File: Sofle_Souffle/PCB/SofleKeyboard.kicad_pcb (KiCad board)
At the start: 2 copper layers, 143.3 x 111.7 mm, 91 parts, among them J2 4PIN, J3 OLED, J4 Conn_01x05_Female, P1 i2c_pin, P2 i2c_pin, SW1 SW_PUSH-MX_W_LED, SW10 SW_PUSH-MX_W_LED, SW11 SW_PUSH-MX_W_LED, SW12 SW_PUSH-MX_W_LED, SW13 SW_PUSH-MX_W_LED, SW14 SW_PUSH-MX_W_LED, SW15 SW_PUSH-MX_W_LED, SW16 SW_PUSH-MX_W_LED, SW17 SW_PUSH-MX_W_LED, SW18 SW_PUSH-MX_W_LED, SW19 SW_PUSH-MX_W_LED, SW2 SW_PUSH-MX_W_LED, SW20 SW_PUSH-MX_W_LED, SW21 SW_PUSH-MX_W_LED, SW22 SW_PUSH-MX_W_LED, SW23 SW_PUSH-MX_W_LED, SW24 SW_PUSH-MX_W_LED, SW25 Rotary_Encoder_Switch, SW26 SW_PUSH-MX_W_LED, SW27 SW_PUSH-MX_W_LED, SW28 SW_PUSH-MX_W_LED, SW29 SW_PUSH-MX_W_LED, SW3 SW_PUSH-MX_W_LED, SW30 SW_PUSH-MX_W_LED, SW4 SW_PUSH-MX_W_LED, SW5 SW_PUSH-MX_W_LED, SW6 SW_PUSH-MX_W_LED, SW7 SW_PUSH-MX_W_LED, SW8 SW_PUSH-MX_W_LED, SW9 SW_PUSH-MX_W_LED, U1 ProMicro

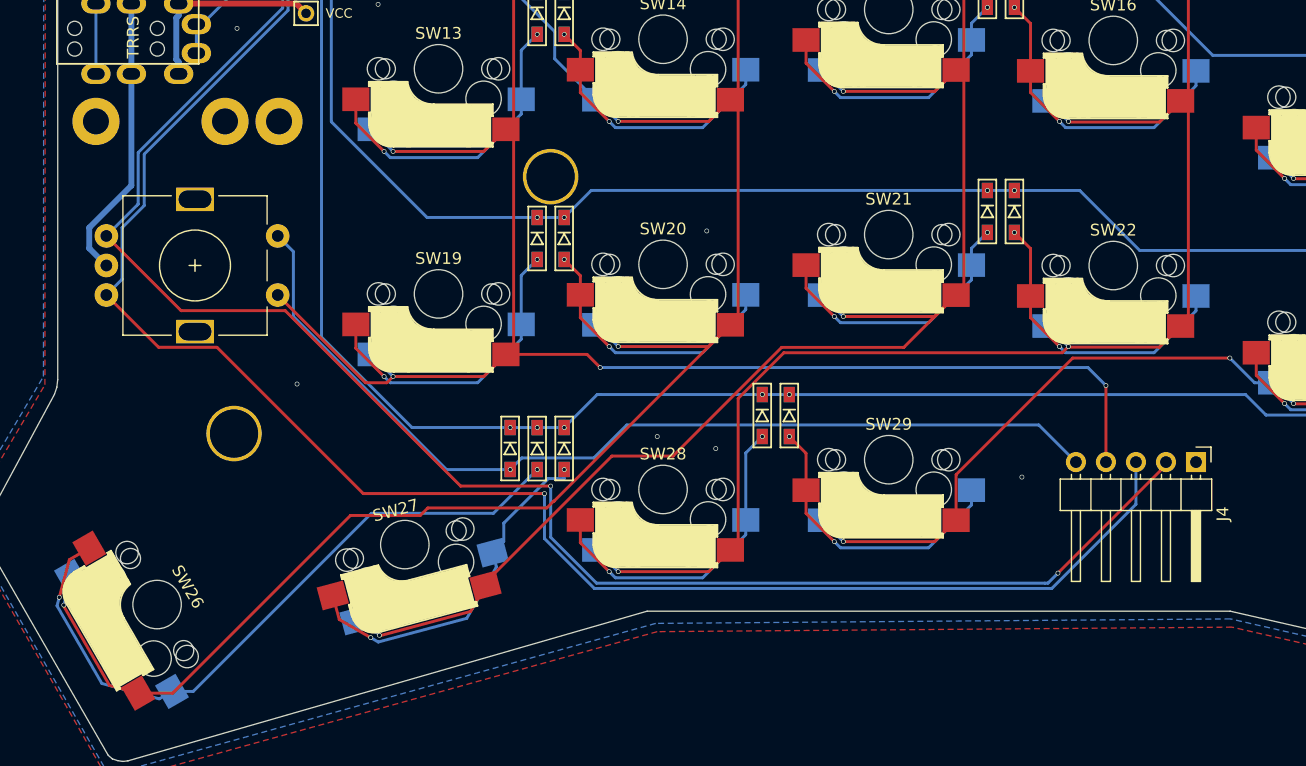
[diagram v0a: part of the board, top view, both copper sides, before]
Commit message: Removed 5pin connector on the right side of the case/pcb.
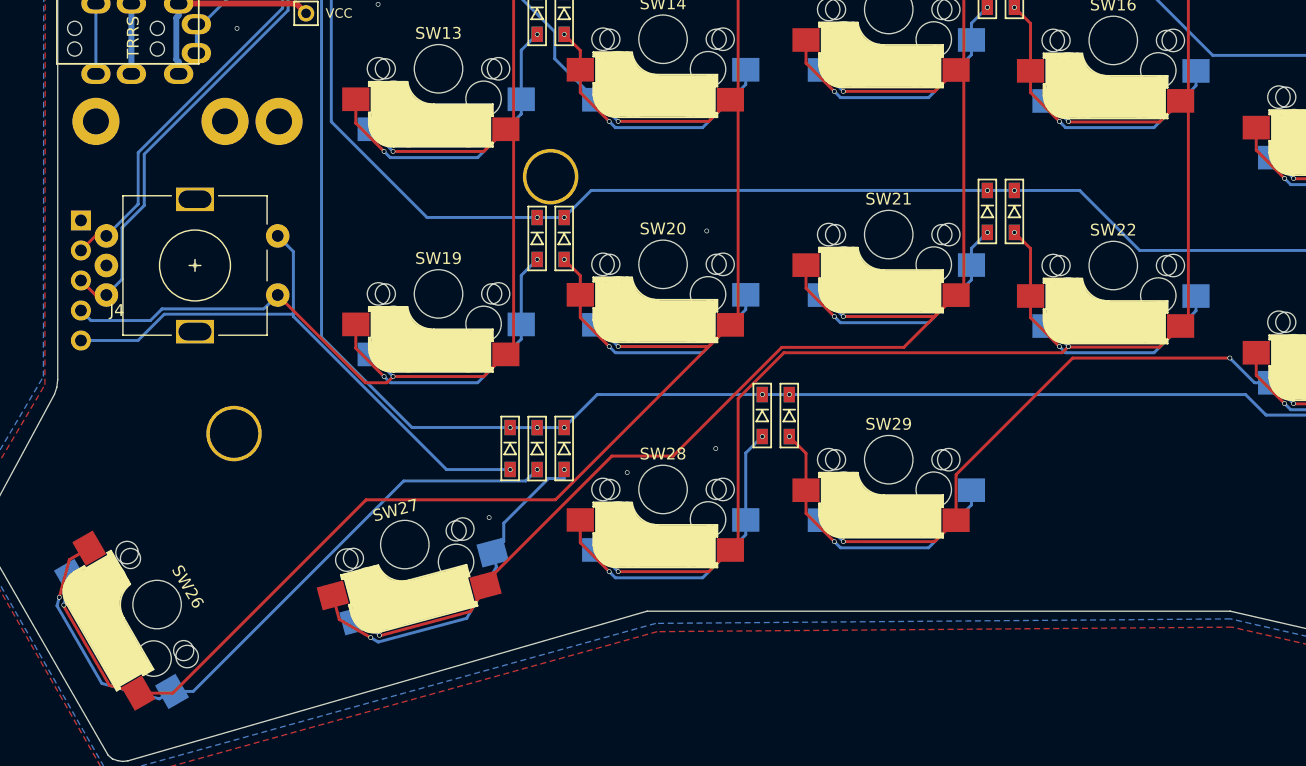
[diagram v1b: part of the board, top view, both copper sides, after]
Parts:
- J4: moved to B.Cu
- moved J4 96.6 mm to (83.6, 103.1), turned to 180 degrees
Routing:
- net ENCA: track 180.9 -> 74.8 mm, vias 3 -> 1
- net ENCB: track 180.9 -> 77.4 mm, vias 2 -> 1
- net SW25A: track 211.5 -> 171.0 mm, vias 6 -> 4
- net SW25B: track 81.8 -> 50.0 mm
- net GND: track 114.2 -> 95.9 mm

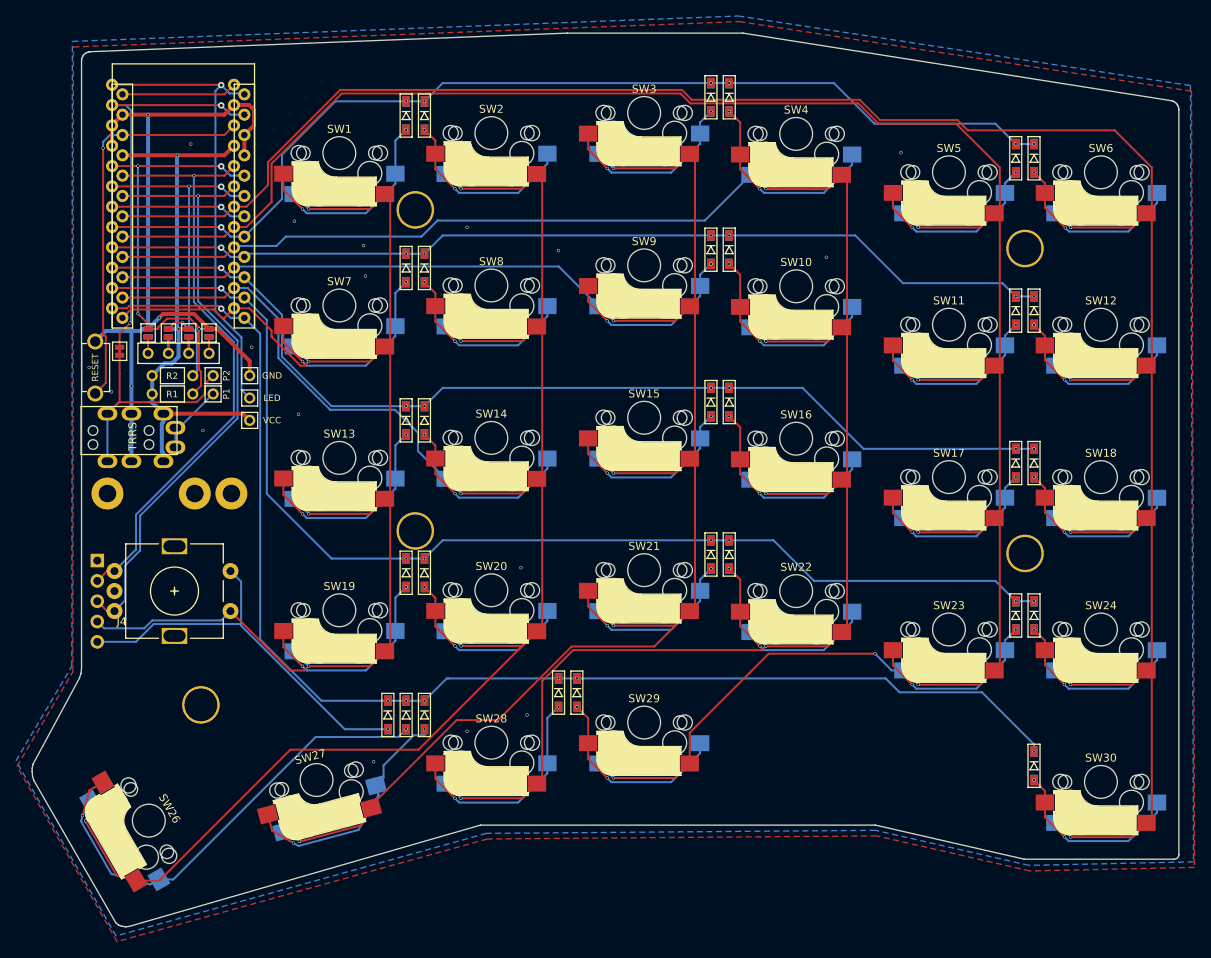
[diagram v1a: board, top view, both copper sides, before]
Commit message: Moved the connector pins for the roller encoder.
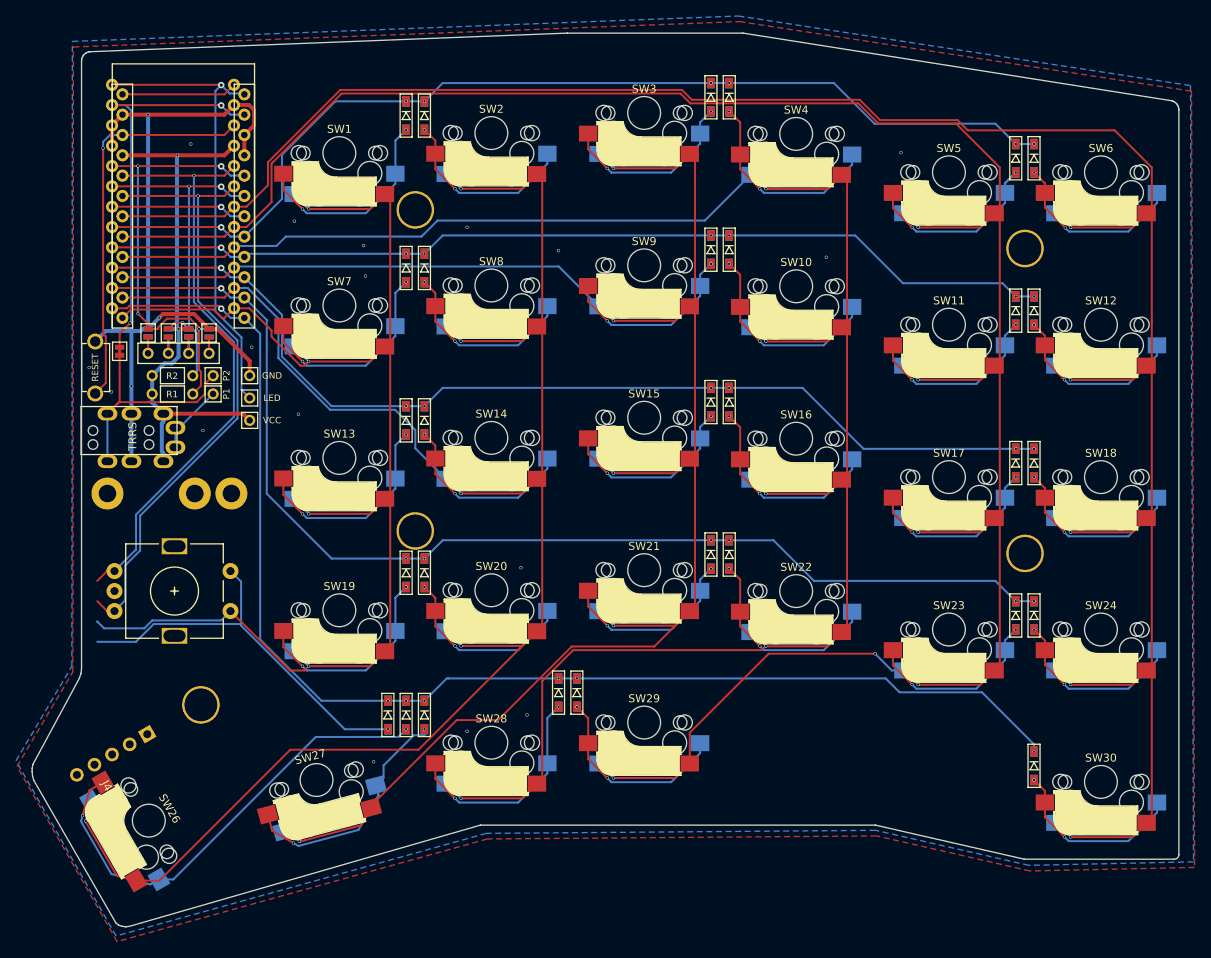
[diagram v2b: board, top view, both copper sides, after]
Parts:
- moved J4 22.6 mm to (89.8, 124.8), turned to 120 degrees
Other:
- net class Default removed
- net class GND removed
- net class VCC removed

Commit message: Moved roller encoder connectors to the same vertical location.
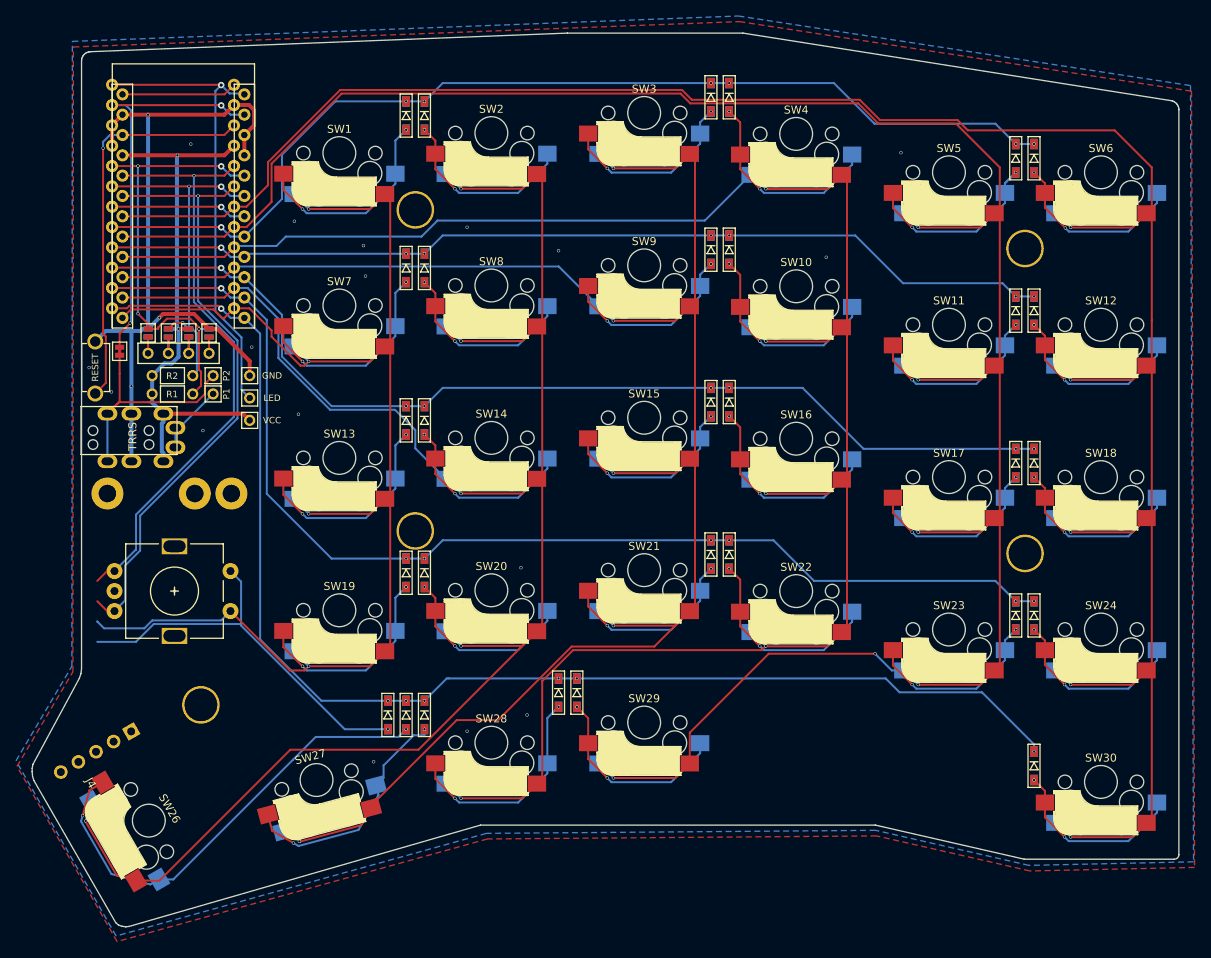
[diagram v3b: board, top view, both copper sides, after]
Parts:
- J4: footprint Connector_PinHeader_2.54mm:PinHeader_1x05_P2.54mm_Horizontal -> SofleRGB:PinHeader_1x05_P2.54mm_Horizontal
- SW1, SW10, SW11, SW12, SW13, SW14, SW15, SW16, SW17, SW18, SW19, SW2, SW20, SW21, SW22, SW23, SW24, SW26, SW27, SW28, SW29, SW3, SW30, SW4, SW5, SW6, SW7, SW8, SW9: footprint SofleRGB:SK6812MINI_and_cherry_NoLEDPads -> SofleRGB:SK6812MINI_and_cherry_NoLEDPads_Narrow_switch_holes
- moved J4 2.04 mm to (87.8, 124.5)

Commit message: Small updates on the PCB and case.
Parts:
- added P3: i2c_pin, SofleRGB:1pin_conn, F.Cu at (97.8, 91.2)
- added P4: i2c_pin, SofleRGB:1pin_conn, F.Cu at (100.6, 91.2)
- added P5: i2c_pin, SofleRGB:1pin_conn, F.Cu at (96.5, 88.4)
- added P6: i2c_pin, SofleRGB:1pin_conn, F.Cu at (99.3, 88.4)
- added P7: i2c_pin, SofleRGB:1pin_conn, F.Cu at (102.1, 88.4)
- added P8: sw_pin, SofleRGB:Single_Hole, F.Cu at (100.8, 99.4)
- added P9: sw_pin, SofleRGB:Single_Hole, F.Cu at (98.2, 99.4)
- added SW25A1: SW_PUSH-MX_W_LED, SofleRGB:SK6812MINI_and_cherry_NoLEDPads, F.Cu at (93.2, 106.9)
- J4: footprint SofleRGB:PinHeader_1x05_P2.54mm_Horizontal -> Connector_PinHeader_2.54mm:PinHeader_1x05_P2.54mm_Horizontal
- SW1, SW10, SW11, SW12, SW13, SW14, SW15, SW16, SW17, SW18, SW19, SW2, SW20, SW21, SW22, SW23, SW24, SW26, SW27, SW28, SW29, SW3, SW30, SW4, SW5, SW6, SW7, SW8, SW9: footprint SofleRGB:SK6812MINI_and_cherry_NoLEDPads_Narrow_switch_holes -> SofleRGB:SK6812MINI_and_cherry_NoLEDPads
- turned SW25 to -90 degrees
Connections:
- U1 pad 24: Net-(U1-Pad24) -> unconnected-(U1-Pad24)
- U1 pad 7: Net-(U1-Pad7) -> unconnected-(U1-Pad7)
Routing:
- net SW25B: track 50.0 -> 88.3 mm, vias 1 -> 2
- net SW25A: track 171.0 -> 207.1 mm
- net ENCA: track 74.8 -> 98.3 mm
- net unconnected-(U1-Pad7): track 0.00 -> 17.0 mm, vias 0 -> 1
- net Net-(U1-Pad7): track 17.0 -> 0.00 mm, vias 1 -> 0
- net ENCB: track 77.4 -> 93.1 mm
- net unconnected-(U1-Pad24): track 0.00 -> 14.4 mm
- net Net-(U1-Pad24): track 14.4 -> 0.00 mm
- net col1: track 288.4 -> 294.4 mm

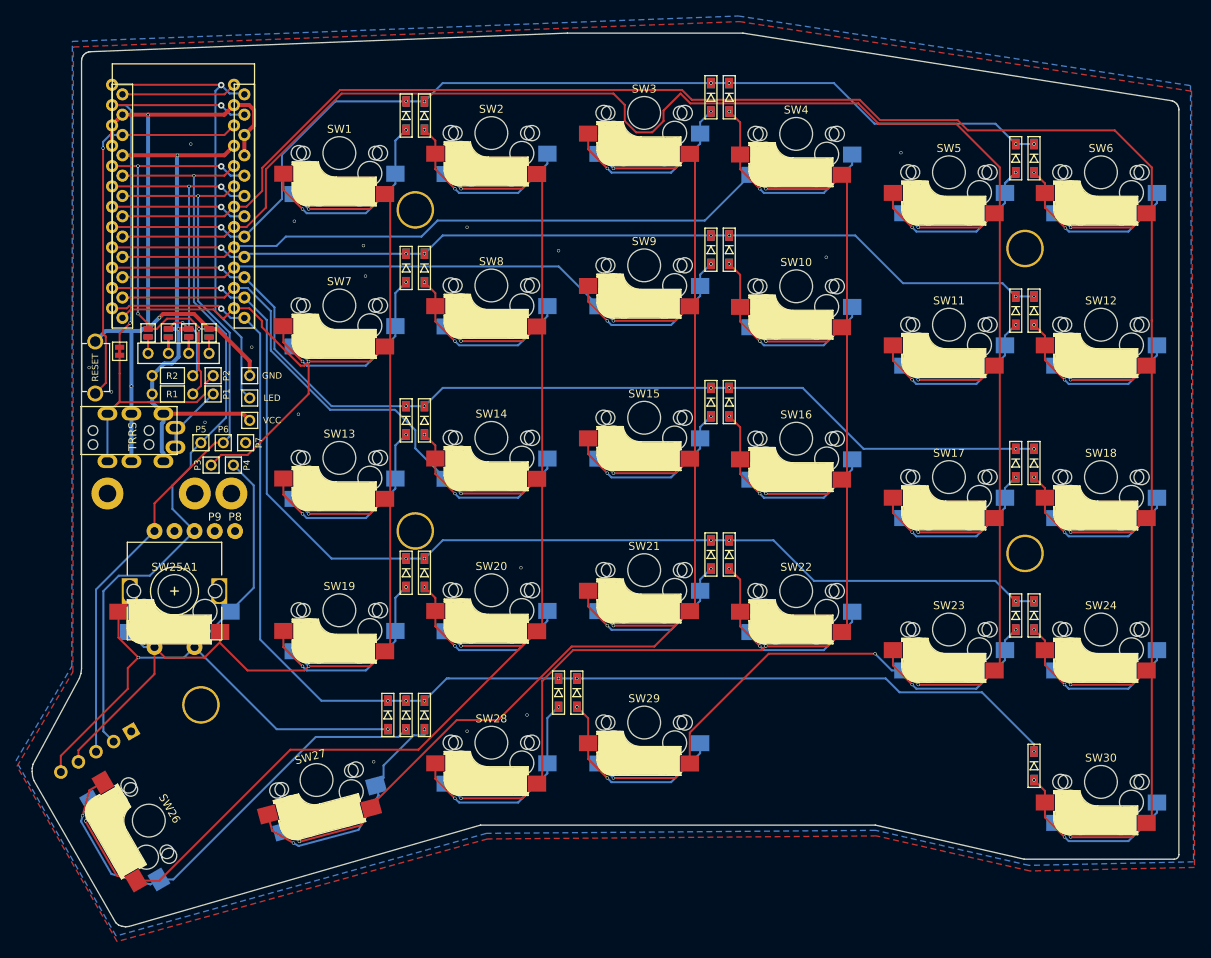
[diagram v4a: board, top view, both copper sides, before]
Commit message: Changed footprint to correct switch holes.
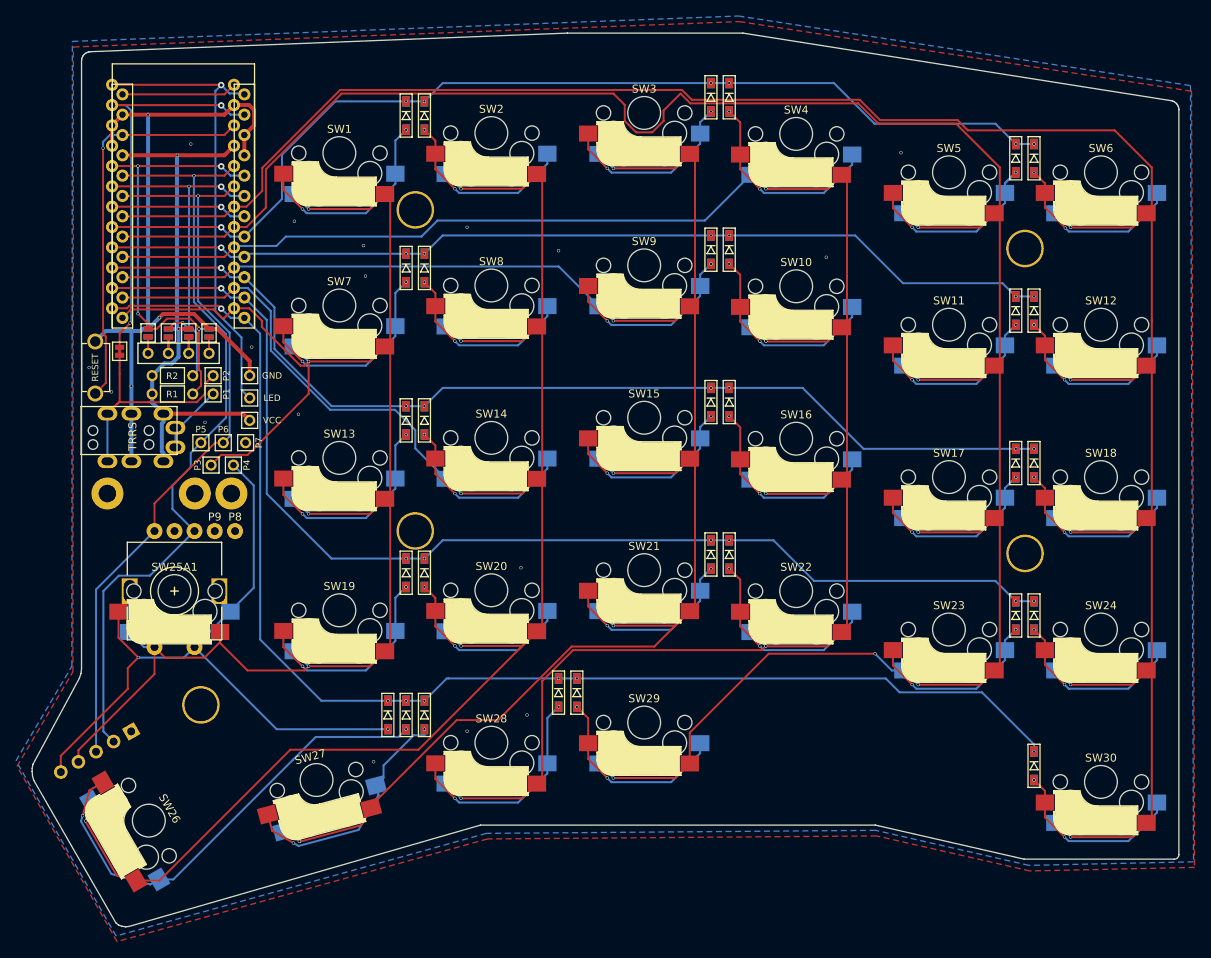
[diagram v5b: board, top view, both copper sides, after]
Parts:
- SW1, SW10, SW11, SW12, SW13, SW14, SW15, SW16, SW17, SW18, SW19, SW2, SW20, SW21, SW22, SW23, SW24, SW25A1, SW26, SW27, SW28, SW29, SW3, SW30, SW4, SW5, SW6, SW7, SW8, SW9: footprint SofleRGB:SK6812MINI_and_cherry_NoLEDPads -> SofleRGB:SK6812MINI_and_cherry_NoLEDPads_corrected_holes
